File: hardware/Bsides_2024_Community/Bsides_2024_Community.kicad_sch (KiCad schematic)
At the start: 44 parts, among them J1 Add_On, J2 Battery, J3 Battery, J4 OLED, J5 Serial_IN, J6 Serial_OUT, P1 USB_C_Plug_USB2.0, Q1 DMG3415U-7, SW1 ON, SW2 RESET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

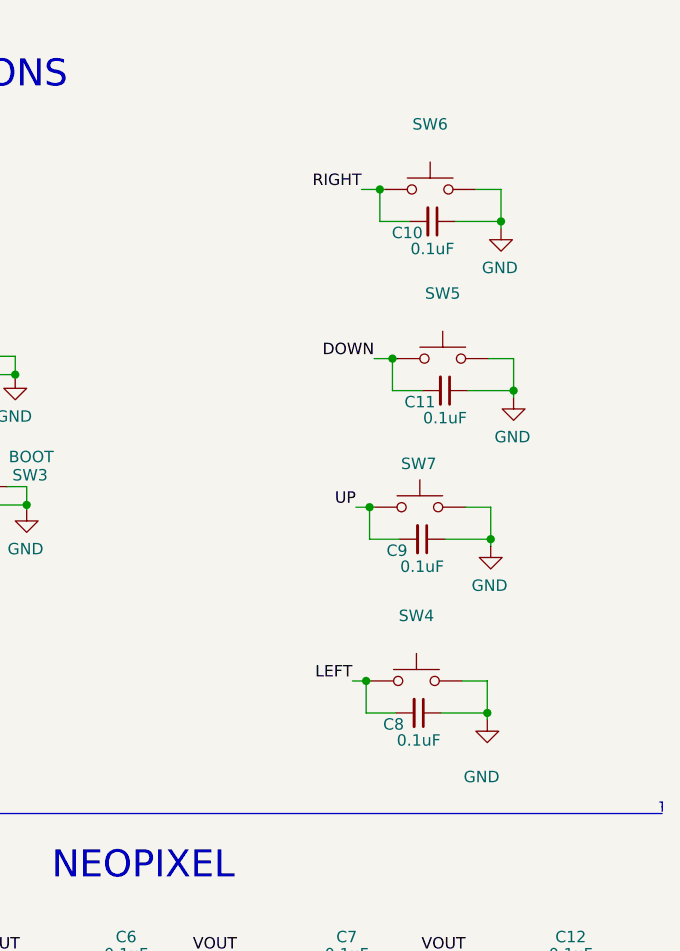
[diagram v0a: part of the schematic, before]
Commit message: feat(Hw): Update route Community
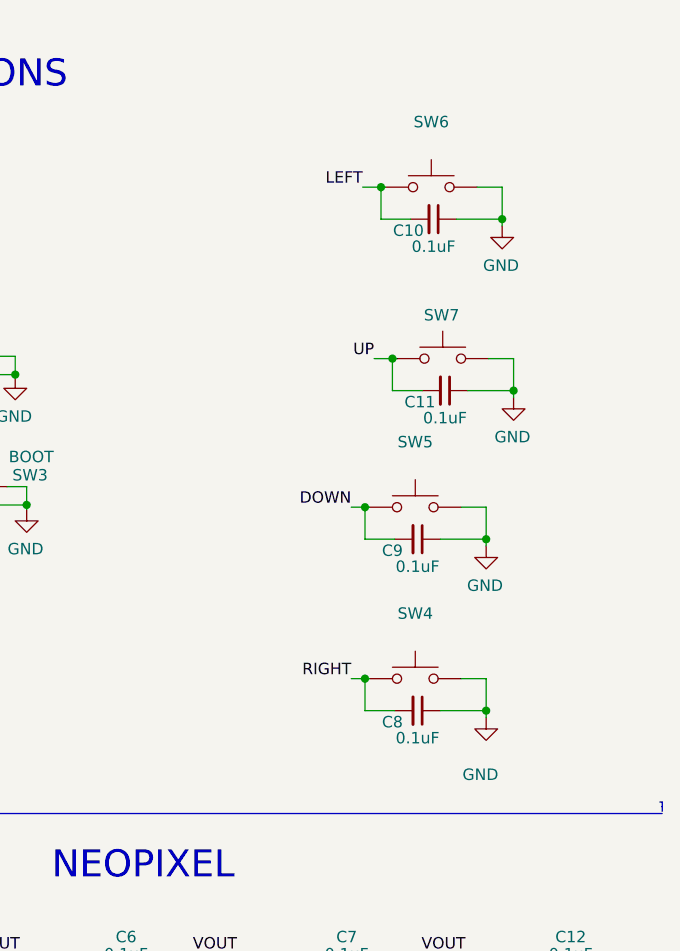
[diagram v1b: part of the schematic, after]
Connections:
- net DOWN: now also C9.2; no longer C11.2
- net LEFT: now also C10.2, SW6.2; no longer C8.2, SW4.2
- net RIGHT: now also C8.2, SW4.2; no longer C10.2, SW6.2
- net UP: now also C11.2; no longer C9.2
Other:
- moved on the sheet: C9, SW5, SW7

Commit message: feat(Hw):Update_PCB_Community
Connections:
- net GPIO16 renamed TX
- net GPIO17 renamed RX
- net GPIO4 renamed RX1
- net GPIO5 renamed TX1
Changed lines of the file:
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@@
 		)
 	)
-	(label "GPIO17"
+	(label "RX"
 		(at 19.05 119.38 0)
 		(fields_autoplaced yes)
@@
 		)
 	)
-	(label "GPIO5"
+	(label "TX1"
 		(at 26.416 43.434 0)
 		(fields_autoplaced yes)
@@
 		)
 	)
-	(label "GPIO4"
+	(label "RX1"
 		(at 135.89 116.84 0)
 		(fields_autoplaced yes)
@@
 		)
 	)
-	(label "GPIO4"
+	(label "RX1"
 		(at 26.416 40.386 0)
 		(fields_autoplaced yes)
@@
 		)
 	)
-	(label "GPIO5"
+	(label "TX1"
 		(at 135.89 119.38 0)
 		(fields_autoplaced yes)
@@
 		)
 	)
-	(label "GPIO16"
+	(label "TX"
 		(at 19.05 116.84 0)
 		(fields_autoplaced yes)
@@
 		)
 	)
-	(label "GPIO17"
+	(label "RX"
 		(at 60.96 68.072 0)
 		(fields_autoplaced yes)
@@
 		)
 	)
-	(label "GPIO16"
+	(label "TX"
 		(at 60.96 65.278 0)
 		(fields_autoplaced yes)
